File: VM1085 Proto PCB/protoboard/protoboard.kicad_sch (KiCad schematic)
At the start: 88 parts, among them J1 Conn_01x03_Male, J10 Conn_01x03_Male, J11 Conn_01x03_Male, J12 Conn_01x03_Male, J13 Conn_01x03_Male, J14 Conn_01x03_Male, J15 Conn_01x03_Male, J16 Conn_01x03_Male, J17 Conn_01x03_Male, J2 Conn_01x08_Female, J3 Conn_01x03_Male, J4 Conn_01x03_Male, J5 Conn_01x03_Male, J6 Conn_01x03_Male, J7 Conn_01x03_Male, J8 Conn_01x03_Male, J9 Conn_01x03_Male, U1 TMUX1134, U10 OPA2145, U2 TMUX1134, U3 TMUX1134, U4 TMUX1134, U5 OPA2145, U6 AD8065, U7 SMD_1.27MM_PROTO_AREA, U8 LT1715, U9 ADG1401

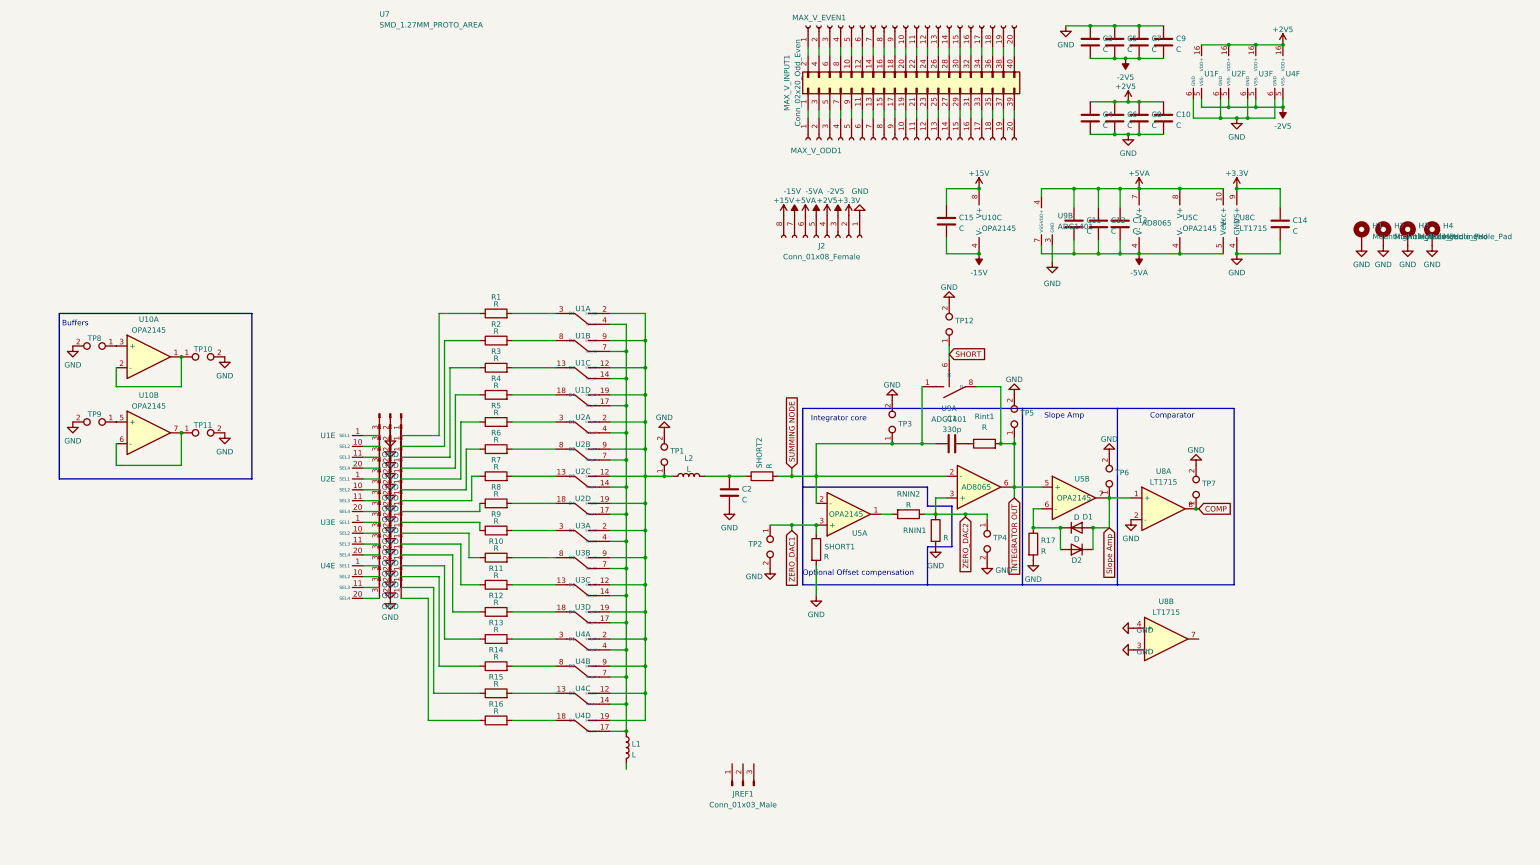
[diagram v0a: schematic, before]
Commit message: added 32 bit runup count and removal of redundant code
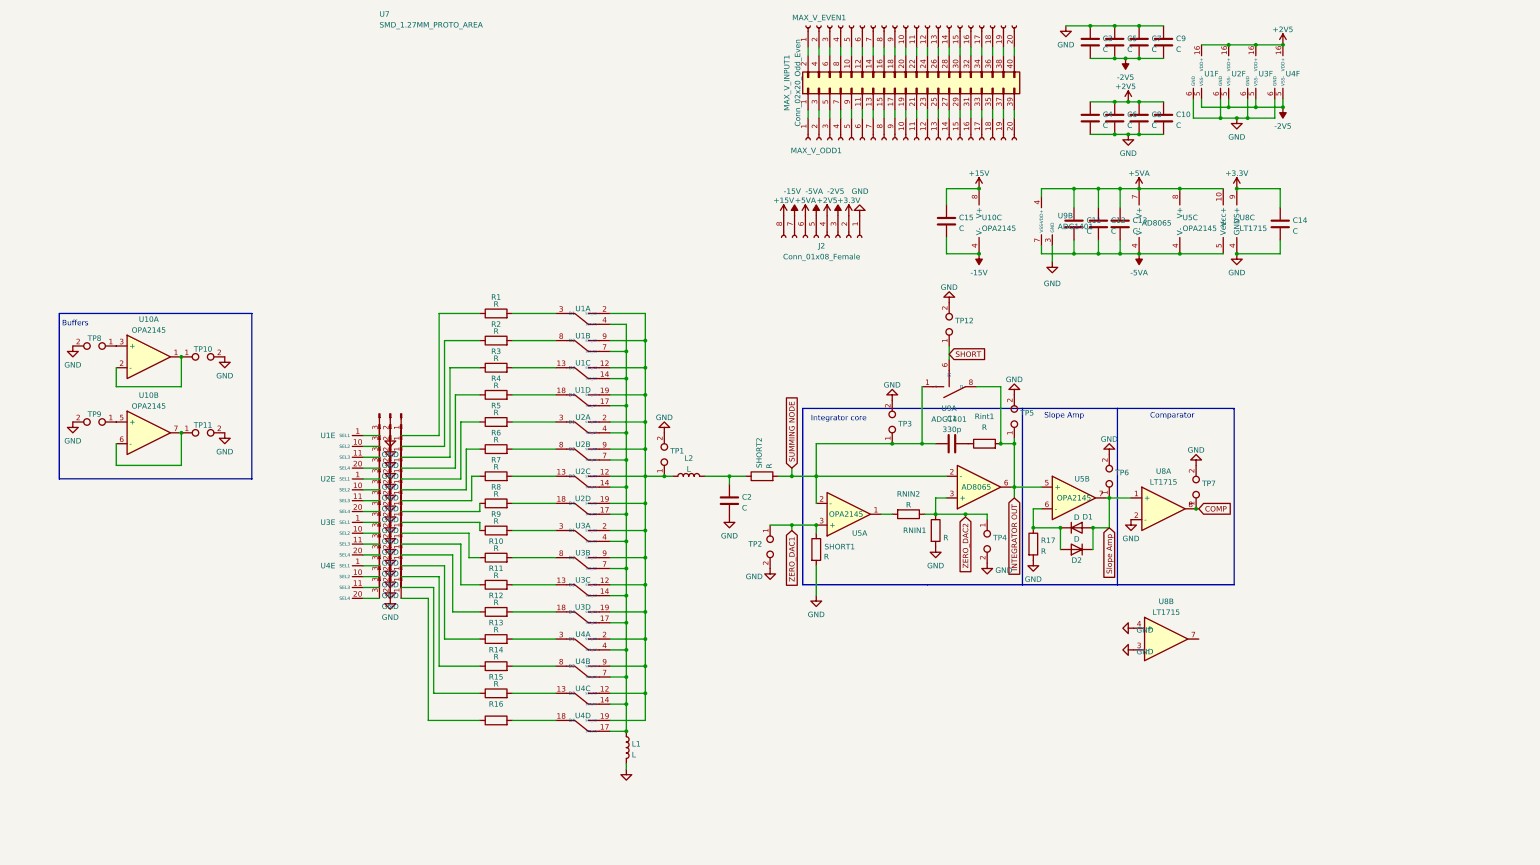
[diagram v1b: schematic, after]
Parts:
- removed H1, H2, H3, H4: MountingHole_Pad, symbol Mechanical:MountingHole_Pad
- removed JREF1: Conn_01x03_Male, symbol Connector:Conn_01x03_Male
- R16: value R -> (none); footprint VM1085:Resistor_multipad -> (none)
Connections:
- net GND: now also L1.2
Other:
- note removed: "Optional Offset compensation"
- moved on the sheet: C2

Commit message: no message
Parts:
- removed L1: L, Capacitor_SMD:C_0805_2012Metric_Pad1.18x1.45mm_HandSolder, symbol Device:L
- R16: value (none) -> R40k; footprint (none) -> VM1085:Resistor_multipad
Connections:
- net GND: now also U1.14 (S3B_NC), U1.17 (S4B_NC), U1.4 (S1B_NC), U1.7 (S2B_NC), U2.14 (S3B_NC), U2.17 (S4B_NC), U2.4 (S1B_NC), U2.7 (S2B_NC), U3.14 (S3B_NC), U3.17 (S4B_NC), U3.4 (S1B_NC), U3.7 (S2B_NC), U4.14 (S3B_NC), U4.17 (S4B_NC), U4.4 (S1B_NC), U4.7 (S2B_NC)
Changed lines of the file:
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@@
   (junction (at 296.545 47.625) (diameter 0) (color 0 0 0 0)
   )
-  (junction (at 182.245 187.325) (diameter 0) (color 0 0 0 0)
-  )
   (junction (at 302.26 40.005) (diameter 0) (color 0 0 0 0)
   )
@@
   (junction (at 182.245 149.225) (diameter 0) (color 0 0 0 0)
   )
+  (junction (at 182.245 187.325) (diameter 0) (color 0 0 0 0)
+  )
   (junction (at 186.69 159.385) (diameter 0) (color 0 0 0 0)
   )
@@
     (stroke (width 0) (type default) (color 0 0 0 0))
   )
-  (wire (pts (xy 182.245 194.945) (xy 182.245 196.215))
+  (wire (pts (xy 182.245 187.325) (xy 182.245 196.215))
     (stroke (width 0) (type default) (color 0 0 0 0))
   )
@@
     (pin "2")
   )
-  (symbol (lib_id "Device:L") (at 182.245 191.135 0) (unit 1)
-    (in_bom yes) (on_board yes) (fields_autoplaced)
-    (property "Reference" "L1" (id 0) (at 183.515 190.3003 0)
-      (effects (font (size 1.27 1.27)) (justify left))
-    )
-    (property "Value" "L" (id 1) (at 183.515 192.8372 0)
-      (effects (font (size 1.27 1.27)) (justify left))
-    )
-    (property "Footprint" "Capacitor_SMD:C_0805_2012Metric_Pad1.18x1.45mm_HandSolder" (id 2) (at 182.245 191.135 0)
-      (effects (font (size 1.27 1.27)) hide)
-    )
-    (property "Datasheet" "~" (id 3) (at 182.245 191.135 0)
-      (effects (font (size 1.27 1.27)) hide)
-    )
-    (pin "1")
-    (pin "2")
-  )
   (symbol (lib_id "Connector_Generic:Conn_02x20_Odd_Even") (at 247.65 36.83 90) (unit 1)
     (in_bom yes) (on_board yes) (fields_autoplaced)
@@
       (effects (font (size 1.27 1.27)) hide)
     )
-    (property "Value" "" (id 1) (at 182.245 200.6584 0))
+    (property "Value" "GND" (id 1) (at 182.245 200.6584 0))
     (property "Footprint" "" (id 2) (at 182.245 196.215 0)
       (effects (font (size 1.27 1.27)) hide)
@@
     (in_bom yes) (on_board yes)
     (property "Reference" "R16" (id 0) (at 151.765 180.975 90))
-    (property "Value" "" (id 1) (at 151.765 182.6061 90))
-    (property "Footprint" "" (id 2) (at 151.765 186.563 90)
+    (property "Value" "R40k" (id 1) (at 151.765 182.6061 90))
+    (property "Footprint" "VM1085:Resistor_multipad" (id 2) (at 151.765 186.563 90)
       (effects (font (size 1.27 1.27)) hide)
     )
@@
       (reference "J17") (unit 1) (value "Conn_01x03_Male") (footprint "Connector_PinHeader_2.54mm:PinHeader_1x03_P2.54mm_Vertical")
     )
-    (path "/4de69147-eb99-460f-95d6-19e0fc7dde03"
-      (reference "L1") (unit 1) (value "L") (footprint "Capacitor_SMD:C_0805_2012Metric_Pad1.18x1.45mm_HandSolder")
-    )
     (path "/117d287b-d2a3-4538-9a17-15db329d178e"

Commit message: rebase save
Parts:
- removed C2: C, Capacitor_SMD:C_0603_1608Metric_Pad1.08x0.95mm_HandSolder, symbol Device:C
- removed J10, J11, J12, J13, J14, J15, J16, J17: Conn_01x03_Male, Connector_PinHeader_2.54mm:PinHeader_1x03_P2.54mm_Vertical, symbol Connector:Conn_01x03_Male
- removed L2: L, Capacitor_SMD:C_0805_2012Metric_Pad1.18x1.45mm_HandSolder, symbol Device:L
- removed R10, R11, R12, R13, R14, R15, R9: R, VM1085:Resistor_multipad, symbol Device:R
- removed R16: R40k, VM1085:Resistor_multipad, symbol Device:R
- removed Rint1, SHORT2: R, Resistor_SMD:R_0805_2012Metric_Pad1.20x1.40mm_HandSolder, symbol Device:R
- removed TP1: TestPoint_2Pole, Connector_PinHeader_2.54mm:PinHeader_1x02_P2.54mm_Vertical, symbol Connector:TestPoint_2Pole
- removed unit 3 of U3
- removed unit 2 of U3
- removed unit 5 of U3
- removed unit 1 of U3
- removed unit 4 of U3
- removed unit 5 of U4
- removed unit 1 of U4
- removed unit 3 of U4
- removed unit 2 of U4
- removed unit 4 of U4
- R4: value R -> 82K
- R5: value R -> 680k
- R6: value R -> 5.12M
- R7: value R -> 0
- R8: value R -> 50k
- R_input: renamed from R1; value R -> 40k
- R_runup: renamed from R2; value R -> 20k
- R_runup2: renamed from R3; value R -> 20k
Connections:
- net INTEGRATOR OUT: now also C1.2
- net SUMMING NODE: now also U1.12 (S3A_NO), U1.19 (S4A_NO), U1.2 (S1A_NO), U1.9 (S2A_NO), U2.12 (S3A_NO), U2.19 (S4A_NO), U2.2 (S1A_NO), U2.9 (S2A_NO)
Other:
- note added: "Slope Switches"
- moved on the sheet: C1, C10, C11, C12, C13, C14, C15, C3, C4, C5, C6, C7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
